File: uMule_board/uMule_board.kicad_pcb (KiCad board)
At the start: 2 copper layers, 140 x 140 mm, 149 parts, among them J1 12V IN, J10 Conn_01x04, J11 Conn_01x04, J12 Conn_01x04, J13 Conn_01x04, J14 Conn_01x04, J2 Dynamixel, J3 Li-Dar_UART, J4 ESP32_UART, J5 Conn_ST_STDC14, J6 I2C, J7 SPI_IMU, J8 Conn_02x04_Odd_Even, J9 Conn_02x04_Odd_Even, P1 BPV10NF, P2 BPV10NF, P3 BPV10NF, P4 BPV10NF, P5 BPV10NF, P6 BPV10NF, P7 BPV10NF, P8 BPV10NF, Q1 AON6407, Q2 S9015, SW1 DBG_BUTT, SW2 RST, U1 TPS62933, U10 OPA397DBVR, U11 OPA397DBVR, U12 OPA397DBVR, U13 OPA397DBVR, U14 OPA397DBVR, U15 OPA397DBVR, U16 SP3485CN, U2 TLV761, U3 LM431BMC3, U4 INA219AxD, U5 TPS62933, U6 STM32F103RCTx, U7 FM24C64B, U8 OPA397DBVR, U9 OPA397DBVR, Y1 8MHz

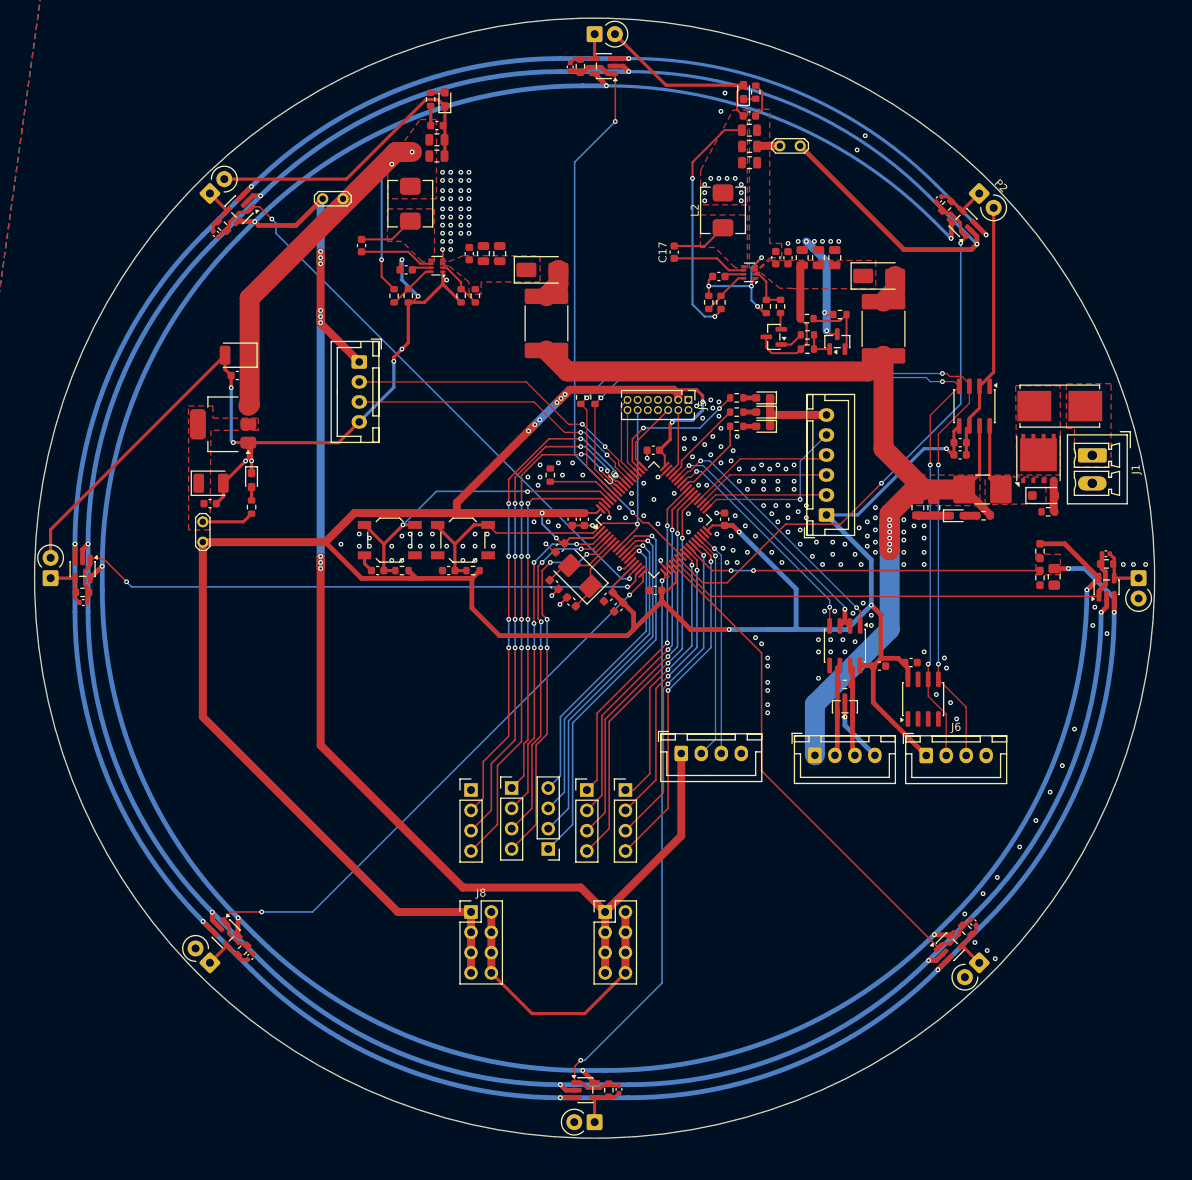
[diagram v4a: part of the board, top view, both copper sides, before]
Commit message: Added descriptions and teardrops. Ready for JLCPCB
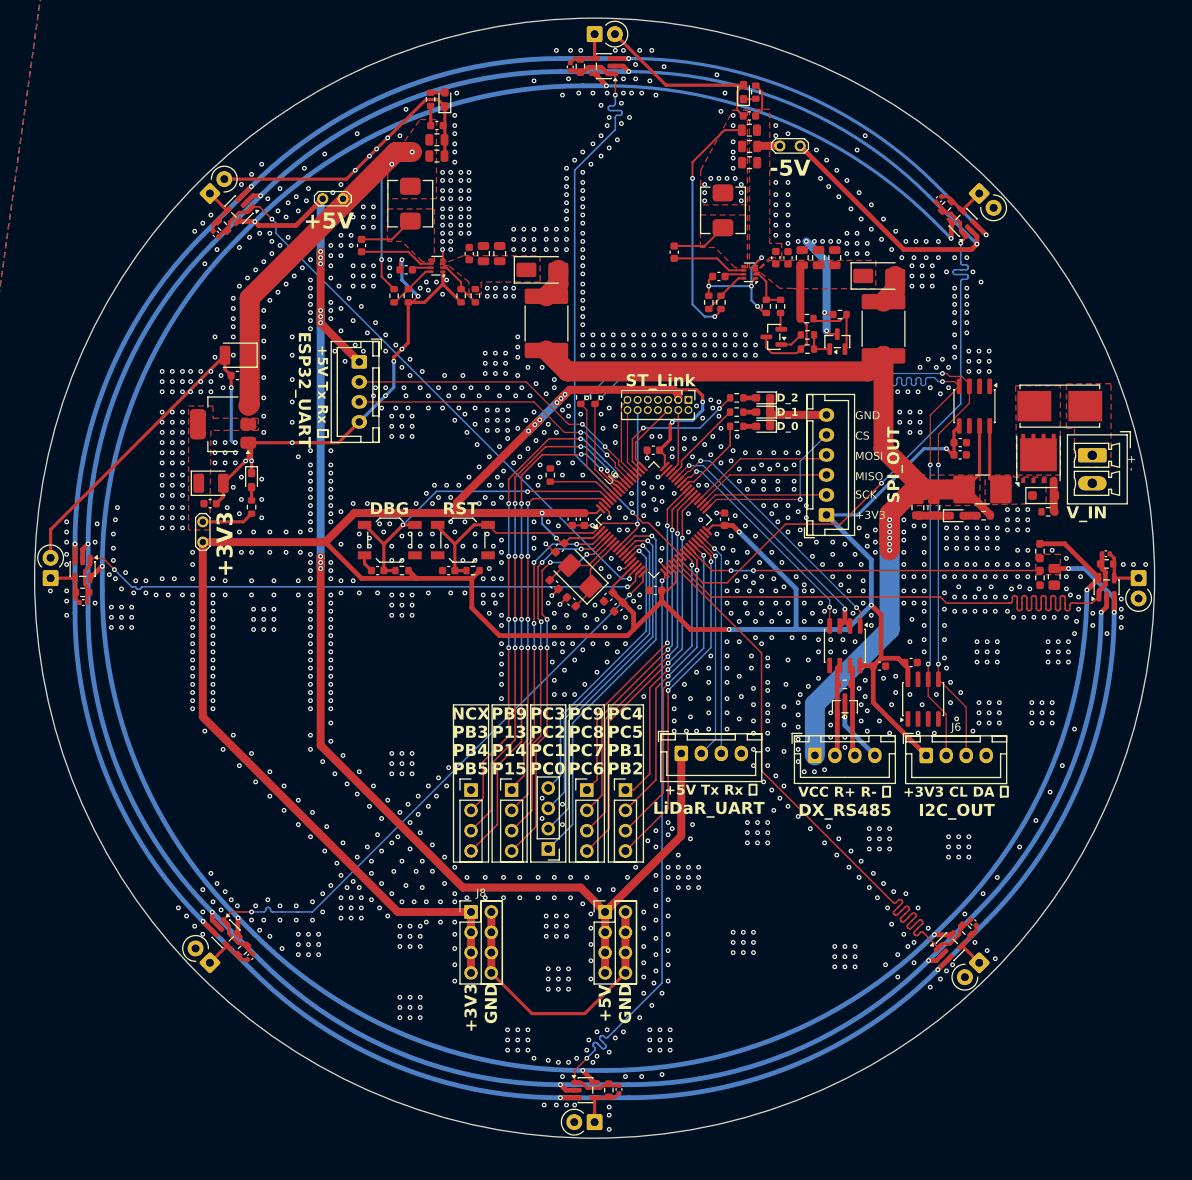
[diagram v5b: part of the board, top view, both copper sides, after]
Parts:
- added G***: LOGO, My_Footprints:QR_N, B.Cu at (138.7, 73.0)
- added G***: LOGO, My_Footprints:B_Łecina, B.Cu at (155.4, 158.8)
- moved J11 0.25 mm to (117.6, 141.7)
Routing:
- net GND: track 330.4 -> 296.2 mm, vias 261 -> 1732
- net /Photodiodes/PHO_2: track 60.5 -> 80.6 mm
- net /Photodiodes/PHO_3: track 67.4 -> 80.6 mm
- net /MCU/I2C1_SCL: track 108.2 -> 114.4 mm
- net /Photodiodes/PHO_1: track 72.8 -> 77.6 mm
- net /Photodiodes/PHO_4: track 74.5 -> 77.6 mm
- net /Photodiodes/PHO_0: track 74.3 -> 77.1 mm
- net /Photodiodes/PHO_7: track 75.0 -> 77.7 mm
- net +3V3: track 387.4 -> 388.3 mm
- net /Photodiodes/PHO_5: track 76.9 -> 77.6 mm
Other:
- board text added: "+ -"
- board text added: "+3V3"
- board text added: "+3V3 CL DA ⏚"
- board text added: "+5V"
- board text added: "+5V Tx Rx ⏚"
- board text added: "-5V"
- board text added: "CS"
- board text added: "DBG"
- board text added: "DX_RS485"
- board text added: "D_0"
- board text added: "D_1"
- board text added: "D_2"
- board text added: "ESP32_UART"
- board text added: "GND"
- board text added: "I2C_OUT"
- board text added: "LiDaR_UART"
- board text added: "MISO"
- board text added: "MOSI"
- board text added: "NCX"
- board text added: "P13"
- board text added: "P14"
- board text added: "P15"
- board text added: "PB1"
- board text added: "PB2"
- board text added: "PB3"
- board text added: "PB4"
- board text added: "PB5"
- board text added: "PB9"
- board text added: "PC0"
- board text added: "PC1"
- board text added: "PC2"
- board text added: "PC3"
- board text added: "PC4"
- board text added: "PC5"
- board text added: "PC6"
- board text added: "PC7"
- board text added: "PC8"
- board text added: "PC9"
- board text added: "RST"
- board text added: "SCK"
- board text added: "SPI_OUT"
- board text added: "ST_Link"
- board text added: "VCC R+ R- ⏚"
- board text added: "V_IN"
- board text added: "uMule_Mainboard V1.0 Author: Oliwier Woźniak"
- board text added: "{dblquote}Co to za filozoia skręcić dwa kabelki?{dblquote}"
- board text added: "~B. Łęcina"

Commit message: initial board is ready for conecting
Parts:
- removed J14: Conn_01x04, Connector_PinHeader_2.54mm:PinHeader_1x04_P2.54mm_Vertical
- removed U6: STM32F103RCTx, Package_QFP:LQFP-64_10x10mm_P0.5mm
- added C51: 100n, Capacitor_SMD:C_0603_1608Metric, F.Cu at (143.5, 115.1)
- added C52: 1u, Capacitor_SMD:C_0603_1608Metric, F.Cu at (143.5, 118.1)
- added R38: 2.2k, Resistor_SMD:R_0603_1608Metric, F.Cu at (148.3, 93.2)
- added R39: 2.2k, Resistor_SMD:R_0603_1608Metric, F.Cu at (149.9, 93.2)
- added U17: STM32G474RETx, Package_QFP:LQFP-64_10x10mm_P0.5mm, F.Cu at (135.4, 107.9)
- moved J4 58.0 mm to (138.7, 130.0), turned to 0 degrees
- moved D8 43.8 mm to (106.5, 103.4), turned to 0 degrees
- moved D9 43.1 mm to (106.5, 101.6), turned to 0 degrees
- moved D10 42.7 mm to (106.5, 99.8), turned to 0 degrees
- moved R24 37.5 mm to (109.8, 103.4), turned to 180 degrees
- moved R25 36.6 mm to (109.8, 101.6), turned to 180 degrees
- moved R26 36.1 mm to (109.8, 99.8), turned to 180 degrees
- moved R21 19.1 mm to (145.3, 93.2)
- moved R20 18.8 mm to (146.8, 93.2)
- moved C29 17.5 mm to (135.4, 99.3)
- moved C30 17.3 mm to (144.0, 107.9), turned to 90 degrees
- moved C35 13.9 mm to (143.5, 116.6), turned to 180 degrees
- moved C34 13.6 mm to (143.5, 113.5), turned to 180 degrees
- moved C33 13.6 mm to (124.7, 107.7), turned to -90 degrees
- moved C32 13.3 mm to (135.4, 117.9), turned to 0 degrees
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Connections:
- J11 pad 2: /GPIO/GPIO_18 -> unconnected-(J11-Pin_2-Pad2)
- J11 pad 3: /GPIO/GPIO_19 -> unconnected-(J11-Pin_3-Pad3)
- J6 pad 2: /MCU/I2C1_SCL -> /Communication/I2C_SCL
- J6 pad 3: /MCU/I2C1_SDA -> /Communication/I2C_SDA
- R20 pad 2: /MCU/I2C1_SCL -> /MCU/PC8/I2C3_SCL
- R21 pad 2: /MCU/I2C1_SDA -> /MCU/PC9/I2C3_SDA
- U4 pad 3: /MCU/I2C1_SDA -> /MCU/PC9/I2C3_SDA
- U4 pad 4: /MCU/I2C1_SCL -> /MCU/PC8/I2C3_SCL
- U7 pad 5: /MCU/I2C1_SDA -> /MCU/PC9/I2C3_SDA
- U7 pad 6: /MCU/I2C1_SCL -> /MCU/PC8/I2C3_SCL
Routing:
- net /MCU/I2C1_SCL: track 114.4 -> 0.00 mm, vias 4 -> 0
- net /MCU/I2C1_SDA: track 113.3 -> 0.00 mm, vias 4 -> 0
- net /Photodiodes/PHO_2: track 80.6 -> 0.00 mm
- net /Photodiodes/PHO_0: track 77.1 -> 0.00 mm, vias 2 -> 0
- net /Photodiodes/PHO_3: track 80.6 -> 5.75 mm
- net GND: track 296.2 -> 224.2 mm, vias 1732 -> 930
- net /Photodiodes/PHO_6: track 77.7 -> 5.75 mm, vias 2 -> 0
- net /Photodiodes/PHO_7: track 77.7 -> 5.75 mm, vias 2 -> 0
- net /Photodiodes/PHO_5: track 77.6 -> 5.75 mm, vias 2 -> 0
- net /Photodiodes/PHO_4: track 77.6 -> 5.75 mm, vias 2 -> 0
- net /Photodiodes/PHO_1: track 77.6 -> 5.75 mm, vias 2 -> 0
- net /GPIO/GPIO_5: track 65.1 -> 0.00 mm, vias 6 -> 0
- net /GPIO/GPIO_4: track 63.9 -> 0.00 mm, vias 6 -> 0
- net /GPIO/GPIO_3: track 62.7 -> 0.00 mm, vias 6 -> 0
- net +3V3: track 388.3 -> 330.6 mm, vias 14 -> 9
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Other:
- board text added: ""Pyk, pyk, pyk, pyk"
- board text removed: "PC0"
- board text removed: "PC1"
- board text removed: "PC2"
- board text removed: "PC3"
